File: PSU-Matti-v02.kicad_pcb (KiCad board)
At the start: 2 copper layers, 100 x 64 mm, 40 parts, among them J1 Screw_Terminal_01x04, U1 LM317_3PinPackage, U2 LM337_TO220

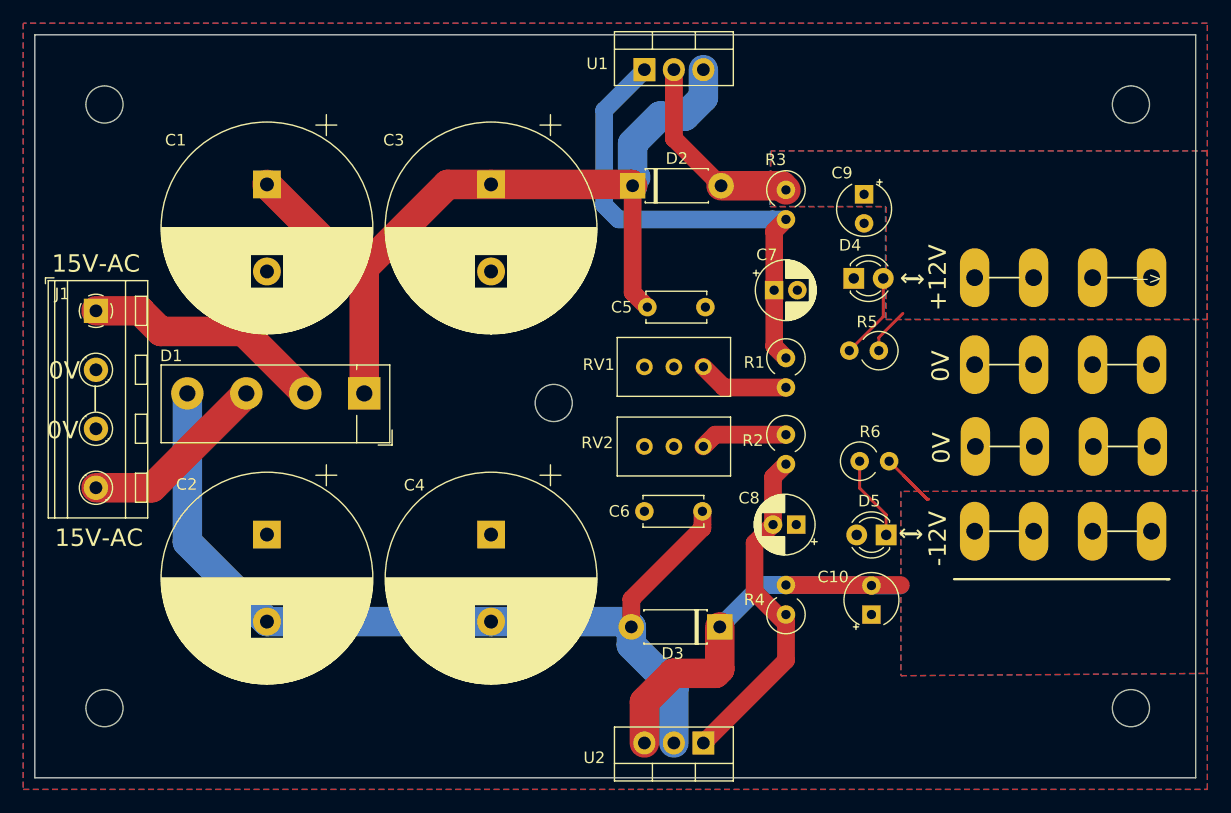
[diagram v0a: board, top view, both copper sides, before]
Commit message: fix
Changed to screw terminals
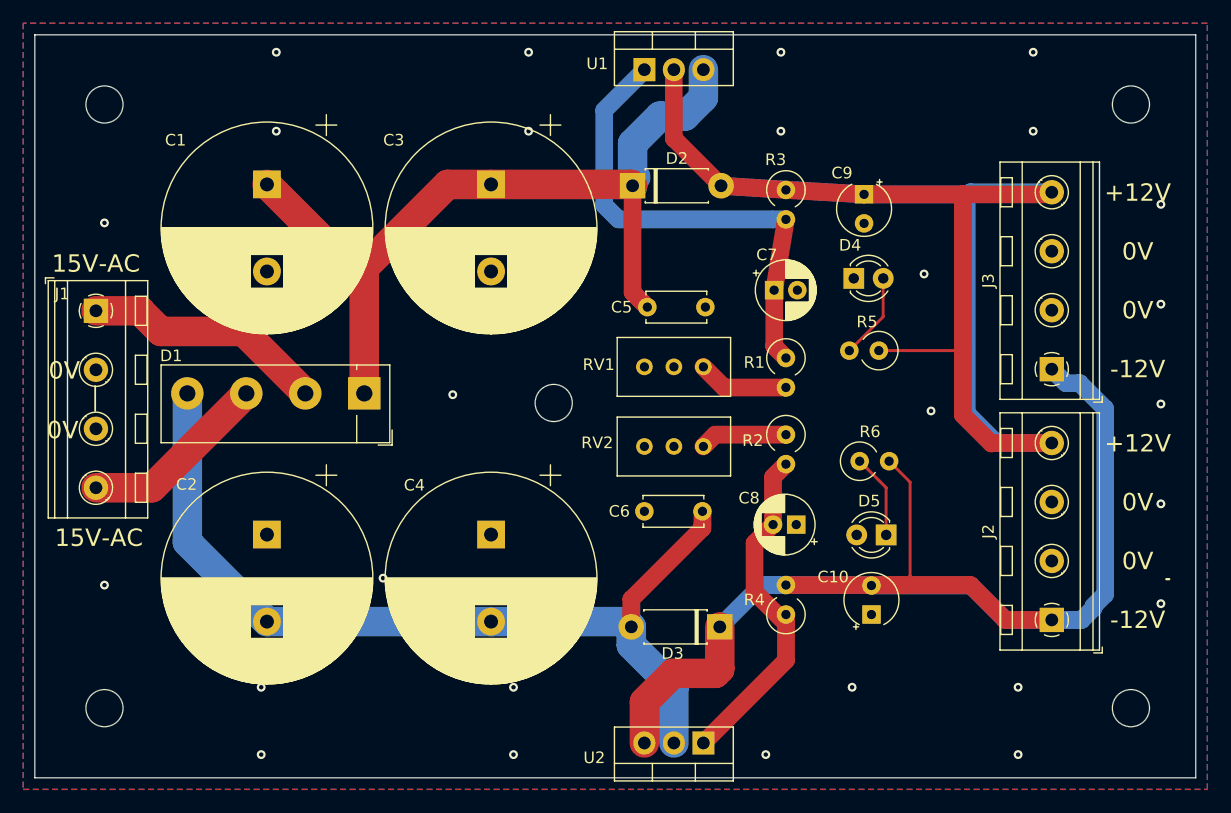
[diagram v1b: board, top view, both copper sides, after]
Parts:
- removed >NAME (x8): , Connector:FASTON_6.35_mm
- added J2: Screw_Terminal_01x04, TerminalBlock_RND:TerminalBlock_RND_205-00234_1x04_P5.08mm_Horizontal, F.Cu at (162.6, 120.4)
- added J3: Screw_Terminal_01x04, TerminalBlock_RND:TerminalBlock_RND_205-00234_1x04_P5.08mm_Horizontal, F.Cu at (162.6, 98.8)
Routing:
- net /+12V: track 21.5 -> 131.0 mm
- net /-12V: track 49.5 -> 109.7 mm
- net /GND: vias 0 -> 27
- removed copper zone on B.Cu, net /+12V
- removed copper zone on F.Cu, net /+12V
- removed copper zone on B.Cu, net /-12V
- removed copper zone on F.Cu, net /-12V
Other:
- board text removed: "—>"
- board text removed: "←"
